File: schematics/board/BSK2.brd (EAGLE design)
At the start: 82 x 100 mm, 34 parts

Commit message: Исправлена БСК1
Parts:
- added C41: 0,1µ, rcl:C0603
- added R1, R2: 2k26, resistor:R0603
- added R75: R01, rcl:R2512
- added R76, R77: 10R, resistor:R0603
- added U$57: INA219AID, CanCubeSat:SOT23-8
- BKU: device pinheadCS:1X08 -> pinheadCS:1X11
- R12, R6: value 2M -> 100k
- R5, R9: value 1M -> 100R
- R94, R95: value 2k26 -> 200k
- moved U$15 15.1 mm to (56.0, 35.0), turned to 315 degrees
- moved U$16 15.1 mm to (26.0, 35.0), turned to 225 degrees
- moved U$6 15.1 mm to (56.0, 65.0), turned to 45 degrees
- moved U$7 15.1 mm to (26.0, 65.0), turned to 135 degrees
- moved R94 2.40 mm to (38.6, 79.6), turned to 0 degrees
- moved R95 2.20 mm to (38.6, 82.0), turned to 0 degrees
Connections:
- net BUS+1 renamed SP+1
- net BUS+2 renamed SP+2
- net BUS+3 renamed SP+3
- net BUS- renamed SP-
- net BUS-1 renamed SP-1
- net BUS-2 renamed SP-2
- net BUS-3 renamed SP-3
- new net 3V3: BKU.8, U$57.4
- new net N$150: C41.1, R76.2, U$57.1
- new net N$151: C41.2, R77.2, U$57.2
- new net N$17: R1.1, R94.2, U$5.1
- new net N$18: R2.1, R95.2, U$5.3
- new net SCL-INA: BKU.10, U$57.5
- new net SDA-INA: BKU.11, U$57.6, U$57.7
- new net SP+: R75.1, R77.1, U$3.1, U$3.2, U$3.3, U$3.4, U$3.P$1, U$3.P$2
- net B2-KVCC: now also R1.2, R2.2; no longer R94.2, R95.2, U$5.1, U$5.3
- net BUS+: now also R75.2, R76.1; no longer U$3.1, U$3.2, U$3.3, U$3.4, U$3.P$1, U$3.P$2
- net GND: now also BKU.9, U$57.3, U$57.8; no longer BKU.8
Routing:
- net BUS+: track 226.1 -> 171.2 mm
- net 2: track 160.0 -> 126.5 mm, vias 2 -> 5
- net SP+: track 0.00 -> 22.0 mm
- net N$17: track 0.00 -> 11.7 mm
- net 5V: track 112.3 -> 118.7 mm
- net GND: track 5.21 -> 11.4 mm
- net SP-: track 117.3 -> 111.2 mm
- net 1W: track 30.4 -> 36.1 mm
- net N$18: track 0.00 -> 4.91 mm
- net B2-ROZE: track 72.6 -> 76.4 mm
- net B2-KHEAT: track 50.0 -> 48.4 mm
- net B2-KVCC: track 35.1 -> 35.7 mm
- net B2-CMD: track 74.1 -> 73.8 mm, vias 2 -> 3
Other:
- outline, holes or cut-outs redrawn

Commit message: Плата АB+DC-DC
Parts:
- moved R77 13.1 mm to (61.1, 84.7), turned to 90 degrees
- moved U$57 11.6 mm to (58.1, 88.4), turned to 90 degrees
- moved R75 9.22 mm to (58.1, 80.8), turned to 180 degrees
- moved C41 7.23 mm to (58.1, 84.7), turned to 0 degrees
- moved R76 2.06 mm to (55.1, 84.7), turned to 90 degrees
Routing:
- net BUS+: track 171.2 -> 217.7 mm
- net 3V3: track 0.00 -> 30.2 mm, vias 0 -> 4
- net SCL-INA: track 0.00 -> 21.6 mm, vias 0 -> 1
- net SDA-INA: track 0.00 -> 20.0 mm, vias 0 -> 1
- net GND: track 11.4 -> 27.5 mm
- net SP-: track 111.2 -> 125.7 mm
- net SP+: track 22.0 -> 29.9 mm
- net N$151: track 0.00 -> 5.39 mm
- net N$150: track 0.00 -> 4.35 mm

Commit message: Изменен номинал резисторов
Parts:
- R13: value 1k5 -> 3k3
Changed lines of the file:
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@@
 </element>
 <element name="U$13" library="CanCubeSat" package="SOT23-3" value="SI2302CDS" x="66.5" y="49.4" smashed="yes"/>
-<element name="R13" library="resistor" library_urn="urn:adsk.eagle:library:348" package="R0603" package3d_urn="urn:adsk.eagle:package:23555/3" value="1k5" x="66.5" y="53.2" smashed="yes">
+<element name="R13" library="resistor" library_urn="urn:adsk.eagle:library:348" package="R0603" package3d_urn="urn:adsk.eagle:package:23555/3" value="3k3" x="66.5" y="53.2" smashed="yes">
 <attribute name="VALUE" x="65.865" y="51.295" size="1.27" layer="27"/>
 </element>

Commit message: Внесены правки в платы БСК
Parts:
- added R3, R32: 100R, resistor:R0603
- moved LED7 2.00 mm to (68.4, 55.6)
- moved R13 2.00 mm to (68.5, 53.2)
- moved R14 2.00 mm to (68.5, 46.6)
- moved U$13 2.00 mm to (68.5, 49.4)
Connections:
- new net N$19: R32.1, R8.1, U$8.1
- new net N$20: R14.1, R3.1, U$13.1
- net B2-KHEAT: now also R32.2; no longer R8.1, U$8.1
- net B2-ROZE: now also R3.2; no longer R14.1, U$13.1
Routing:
- net N$19: track 0.00 -> 4.04 mm
- net BUS+: track 217.7 -> 221.7 mm
- net N$20: track 0.00 -> 3.94 mm
- net 2: track 126.5 -> 129.0 mm
- net B2-KHEAT: track 48.4 -> 47.0 mm
- net B2-ROZE: track 76.4 -> 75.3 mm

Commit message: Две линии i2c на платах БСК заменены на одну
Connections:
- net SCL-INA renamed SCL-TM
- net SDA-INA renamed SDA-TM
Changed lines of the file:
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@@
 <via x="73.9" y="98.9" extent="1-16" drill="1"/>
 </signal>
-<signal name="SCL-INA">
+<signal name="SCL-TM">
 <contactref element="U$57" pad="5"/>
 <contactref element="BKU" pad="10"/>
@@
 <wire x1="59.075" y1="91.2493" x2="59.075" y2="89.7" width="0.3" layer="1"/>
 </signal>
-<signal name="SDA-INA">
+<signal name="SDA-TM">
 <contactref element="U$57" pad="6"/>
 <contactref element="U$57" pad="7"/>

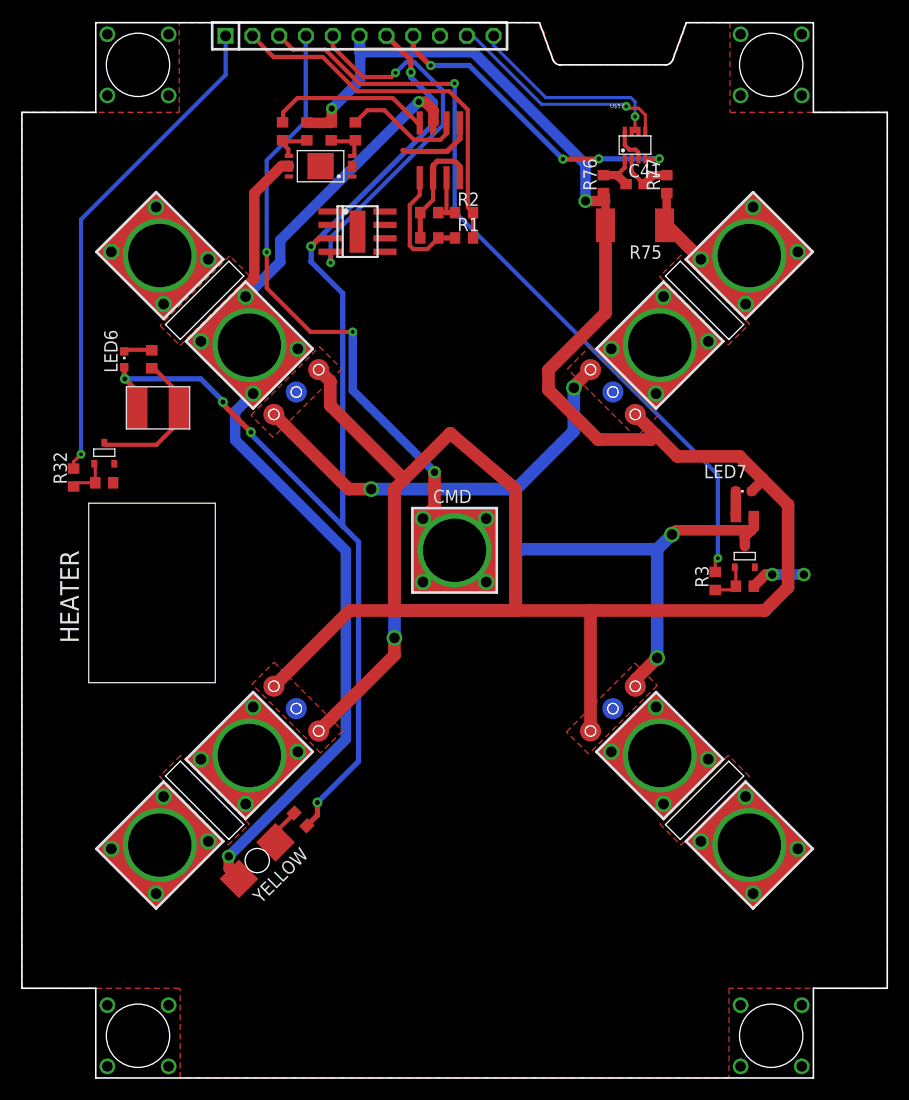
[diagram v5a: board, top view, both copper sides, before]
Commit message: Обновлен список плат, работа над платой ПН
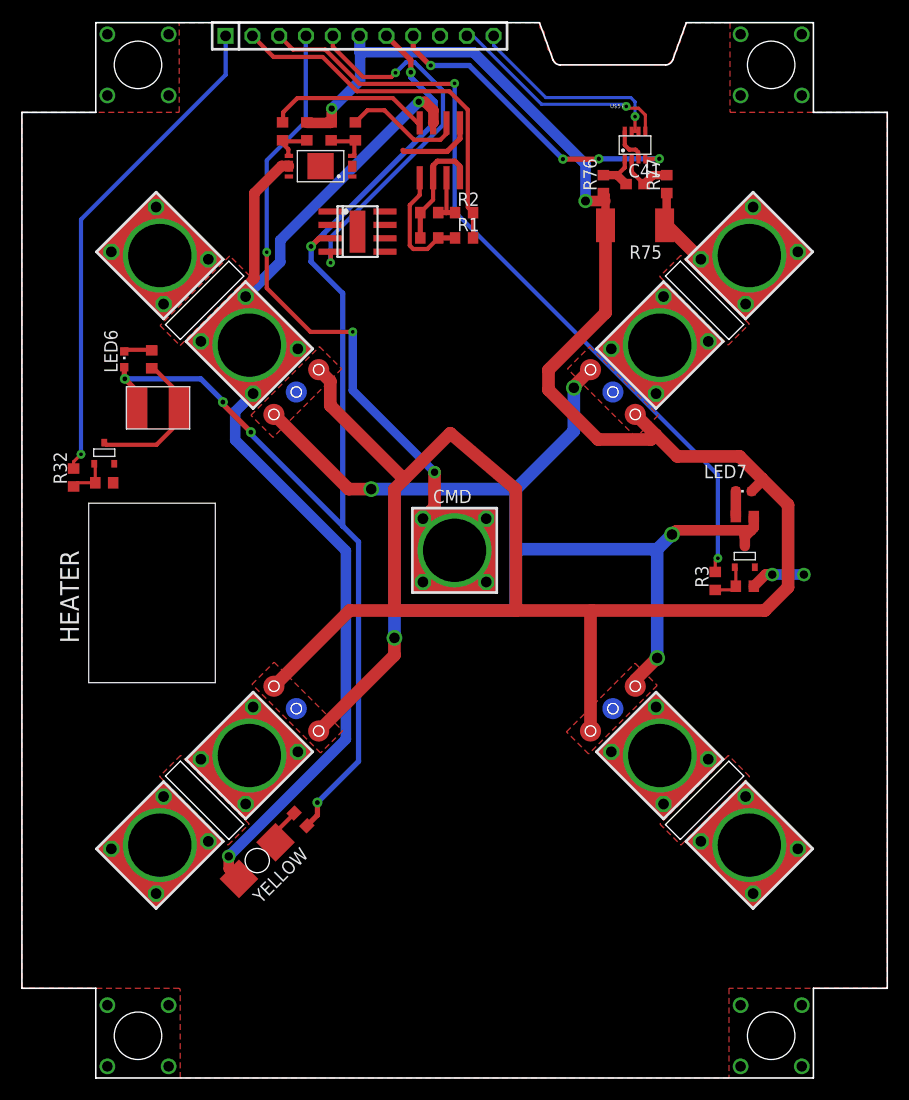
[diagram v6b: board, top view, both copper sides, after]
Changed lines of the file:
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@@
 <wire x1="7" y1="0" x2="7" y2="8.5" width="0.1524" layer="20"/>
 <wire x1="7" y1="8.5" x2="0" y2="8.5" width="0.1524" layer="20"/>
-<hole x="11" y="4" drill="6"/>
+<hole x="11" y="4" drill="4.5"/>
 <wire x1="60.976" y1="24.014" x2="66.986" y2="30.024" width="0.05" layer="20"/>
 <wire x1="66.986" y1="30.024" x2="68.4" y2="28.61" width="0.05" layer="20"/>
@@
 <wire x1="15.014" y1="30.024" x2="21.024" y2="24.014" width="0.05" layer="20"/>
 <wire x1="21.024" y1="24.014" x2="19.61" y2="22.6" width="0.05" layer="20"/>
-<hole x="71" y="4" drill="6"/>
-<hole x="71" y="96" drill="6"/>
-<hole x="11" y="96" drill="6"/>
+<hole x="71" y="4" drill="4.5"/>
+<hole x="71" y="96" drill="4.5"/>
+<hole x="11" y="96" drill="4.5"/>
 <wire x1="49.04" y1="100" x2="50.33" y2="96.47" width="0.1524" layer="20"/>
 <wire x1="50.33" y1="96.47" x2="51" y2="96" width="0.1524" layer="20" curve="69.947894"/>

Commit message: Схема БКУ
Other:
- outline, holes or cut-outs redrawn
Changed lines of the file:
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@@
 <setting verticaltext="up"/>
 </settings>
-<grid distance="0.1" unitdist="mm" unit="mm" style="lines" multiple="1" display="yes" altdistance="0.01" altunitdist="mm" altunit="mm"/>
+<grid distance="1" unitdist="mm" unit="mm" style="lines" multiple="1" display="yes" altdistance="0.01" altunitdist="mm" altunit="mm"/>
 <layers>
 <layer number="1" name="Top" color="4" fill="1" visible="yes" active="yes"/>
@@
 <wire x1="0" y1="91.5" x2="7" y2="91.5" width="0.1524" layer="20"/>
 <wire x1="7" y1="91.5" x2="7" y2="100" width="0.1524" layer="20"/>
-<wire x1="7" y1="100" x2="49.04" y2="100" width="0.1524" layer="20"/>
-<wire x1="62.96" y1="100" x2="75" y2="100" width="0.1524" layer="20"/>
+<wire x1="7" y1="100" x2="49" y2="100" width="0.1524" layer="20"/>
+<wire x1="63" y1="100" x2="75" y2="100" width="0.1524" layer="20"/>
 <wire x1="75" y1="100" x2="75" y2="91.5" width="0.1524" layer="20"/>
 <wire x1="75" y1="91.5" x2="82" y2="91.5" width="0.1524" layer="20"/>
@@
 <hole x="71" y="96" drill="4.5"/>
 <hole x="11" y="96" drill="4.5"/>
-<wire x1="49.04" y1="100" x2="50.33" y2="96.47" width="0.1524" layer="20"/>
-<wire x1="50.33" y1="96.47" x2="51" y2="96" width="0.1524" layer="20" curve="69.947894"/>
-<wire x1="51" y1="96" x2="61" y2="96" width="0.1524" layer="20"/>
-<wire x1="61" y1="96" x2="61.67" y2="96.47" width="0.1524" layer="20" curve="69.947894"/>
-<wire x1="61.67" y1="96.47" x2="62.96" y2="100" width="0.1524" layer="20"/>
 <wire x1="6.328" y1="37.462" x2="6.328" y2="54.462" width="0.1" layer="21"/>
 <wire x1="6.328" y1="54.462" x2="18.328" y2="54.462" width="0.1" layer="21"/>
@@
 <text x="31.6" y="96.1" size="2" layer="26" rot="MR0" align="top-right">to BKU</text>
 <text x="5.4" y="45.6" size="1.778" layer="21" rot="R90" align="bottom-center">HEATER</text>
+<wire x1="49" y1="100" x2="63" y2="100" width="0.1524" layer="20"/>
 </plain>
 <attributes>
@@
 <vertex x="14.9" y="91.5"/>
 <vertex x="14.9" y="100"/>
-<vertex x="49.1" y="100"/>
-<vertex x="49.1" y="99.5"/>
-<vertex x="49.5" y="99.1"/>
-<vertex x="49.5" y="98.4"/>
-<vertex x="49.8" y="98.1"/>
-<vertex x="49.8" y="97.5"/>
-<vertex x="50.2" y="97.1"/>
-<vertex x="50.2" y="96.6"/>
-<vertex x="50.8" y="96"/>
-<vertex x="61.2" y="96"/>
-<vertex x="61.8" y="96.6"/>
-<vertex x="61.8" y="97.1"/>
-<vertex x="62.1" y="97.4"/>
-<vertex x="62.1" y="97.9"/>
-<vertex x="62.4" y="98.2"/>
-<vertex x="62.4" y="98.7"/>
-<vertex x="62.7" y="99"/>
-<vertex x="62.7" y="99.5"/>
-<vertex x="62.9" y="99.7"/>
+<vertex x="49.3665875" y="100"/>
 <vertex x="62.9" y="100"/>
 <vertex x="67.1" y="100"/>
